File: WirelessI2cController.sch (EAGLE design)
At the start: 38 parts, among them CN1 I2C, CN2 I2C, CN3 I2C, CN4 POWER 7.4V, IC1 FT232RQ, IC2 TC7SZ126FU, IC3 TC7SZ126FU, IC4 TWE-001L-NC, IC5 MPU-9250, IC6 MS5611-01BA03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

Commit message: 配線名を変更
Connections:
- removed net RXD2: IC4.DIO9, RN3C.2
- removed net TXD2: IC4.DIO11, RN3B.2
- new net RXD0: IC4.DIO7, RN1C.2
- new net TXD0: IC4.DIO6, RN1B.2
- net RXD1: now also IC4.DIO9, RN3C.2; no longer IC4.DIO7, RN1C.2
- net TXD1: now also IC4.DIO11, RN3B.2; no longer IC4.DIO6, RN1B.2
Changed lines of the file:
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@@
 </segment>
 </net>
-<net name="RXD1" class="0">
+<net name="RXD0" class="0">
 <segment>
 <wire x1="124.46" y1="129.54" x2="129.54" y2="129.54" width="0.1524" layer="91"/>
@@
 </segment>
 </net>
-<net name="TXD1" class="0">
+<net name="TXD0" class="0">
 <segment>
 <wire x1="124.46" y1="121.92" x2="129.54" y2="121.92" width="0.1524" layer="91"/>
@@
 </segment>
 </net>
-<net name="RXD1" class="0">
+<net name="RXD0" class="0">
 <segment>
 <pinref part="IC4" gate="G$1" pin="DIO7"/>
@@
 </segment>
 </net>
-<net name="TXD1" class="0">
+<net name="TXD0" class="0">
 <segment>
 <pinref part="IC4" gate="G$1" pin="DIO6"/>
@@
 </segment>
 </net>
-<net name="RXD2" class="0">
+<net name="RXD1" class="0">
 <segment>
 <pinref part="IC4" gate="G$1" pin="DIO9"/>
@@
 </segment>
 </net>
-<net name="TXD2" class="0">
+<net name="TXD1" class="0">
 <segment>
 <pinref part="IC4" gate="G$1" pin="DIO11"/>
@@
 </segment>
 </net>
-<net name="RXD2" class="0">
+<net name="RXD1" class="0">
 <segment>
 <wire x1="162.56" y1="106.68" x2="167.64" y2="106.68" width="0.1524" layer="91"/>
@@
 </segment>
 </net>
-<net name="TXD2" class="0">
+<net name="TXD1" class="0">
 <segment>
 <wire x1="162.56" y1="99.06" x2="167.64" y2="99.06" width="0.1524" layer="91"/>

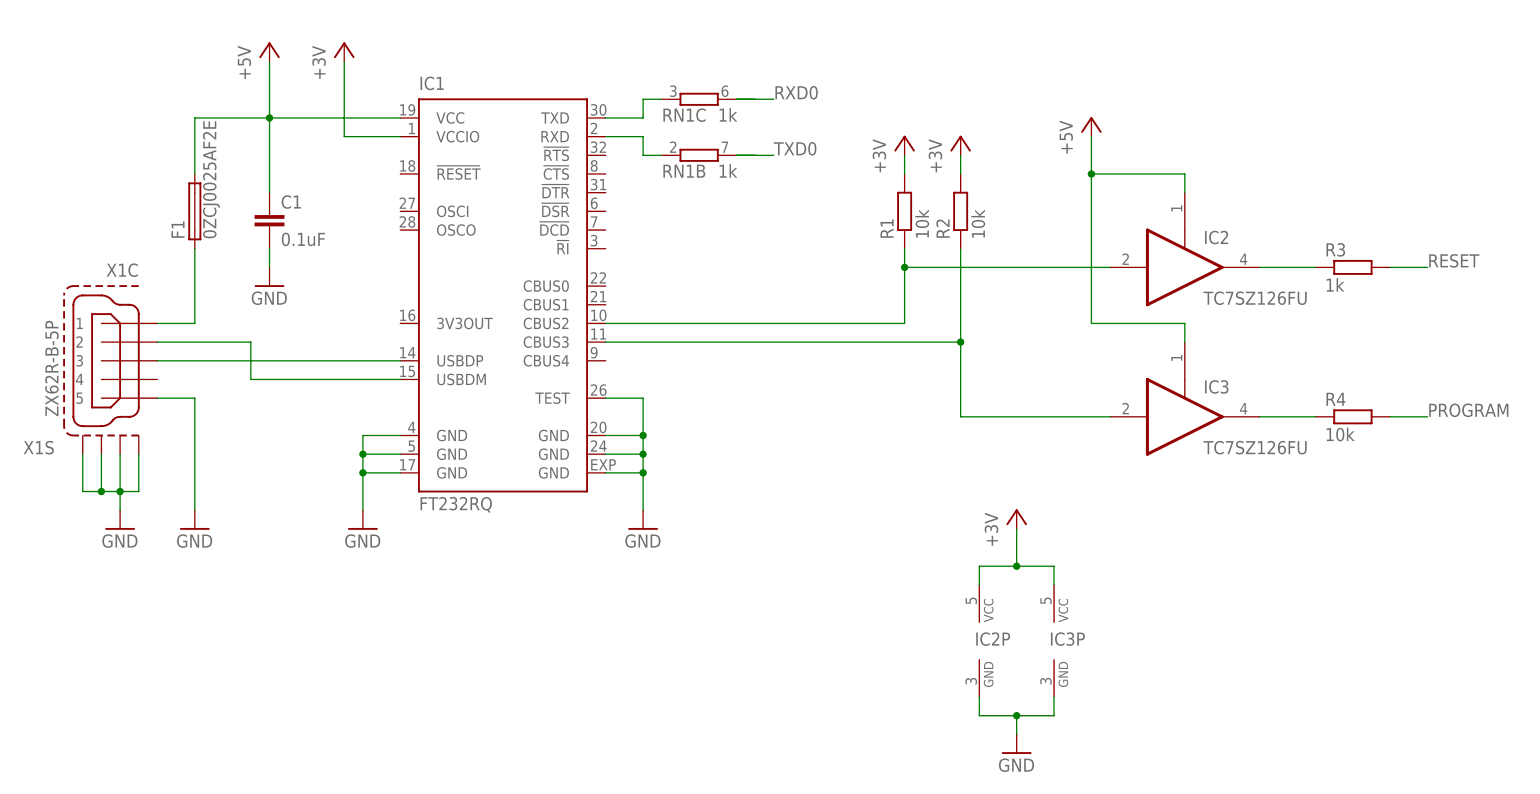
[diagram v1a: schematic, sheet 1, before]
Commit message: 電圧のシンボルを3.3Vに変更
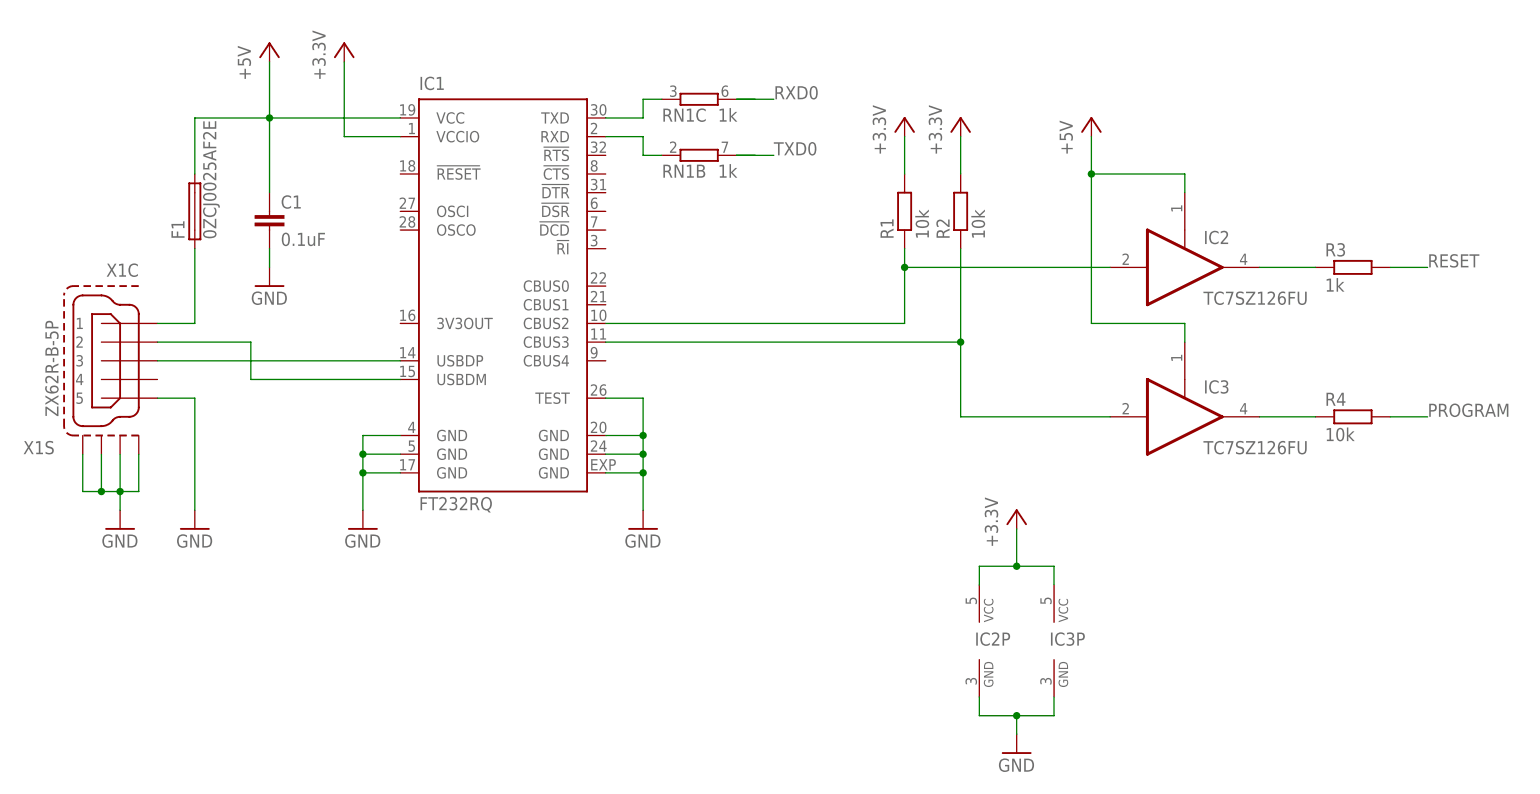
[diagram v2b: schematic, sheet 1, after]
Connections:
- net +3V renamed +3.3V
